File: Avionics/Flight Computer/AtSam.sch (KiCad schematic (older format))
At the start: 42 parts, among them U12 ATSAME70Q21A-AN, Y1 9HT11-32.768KDZB-T, Y2 7V-16.000MAHJ-T

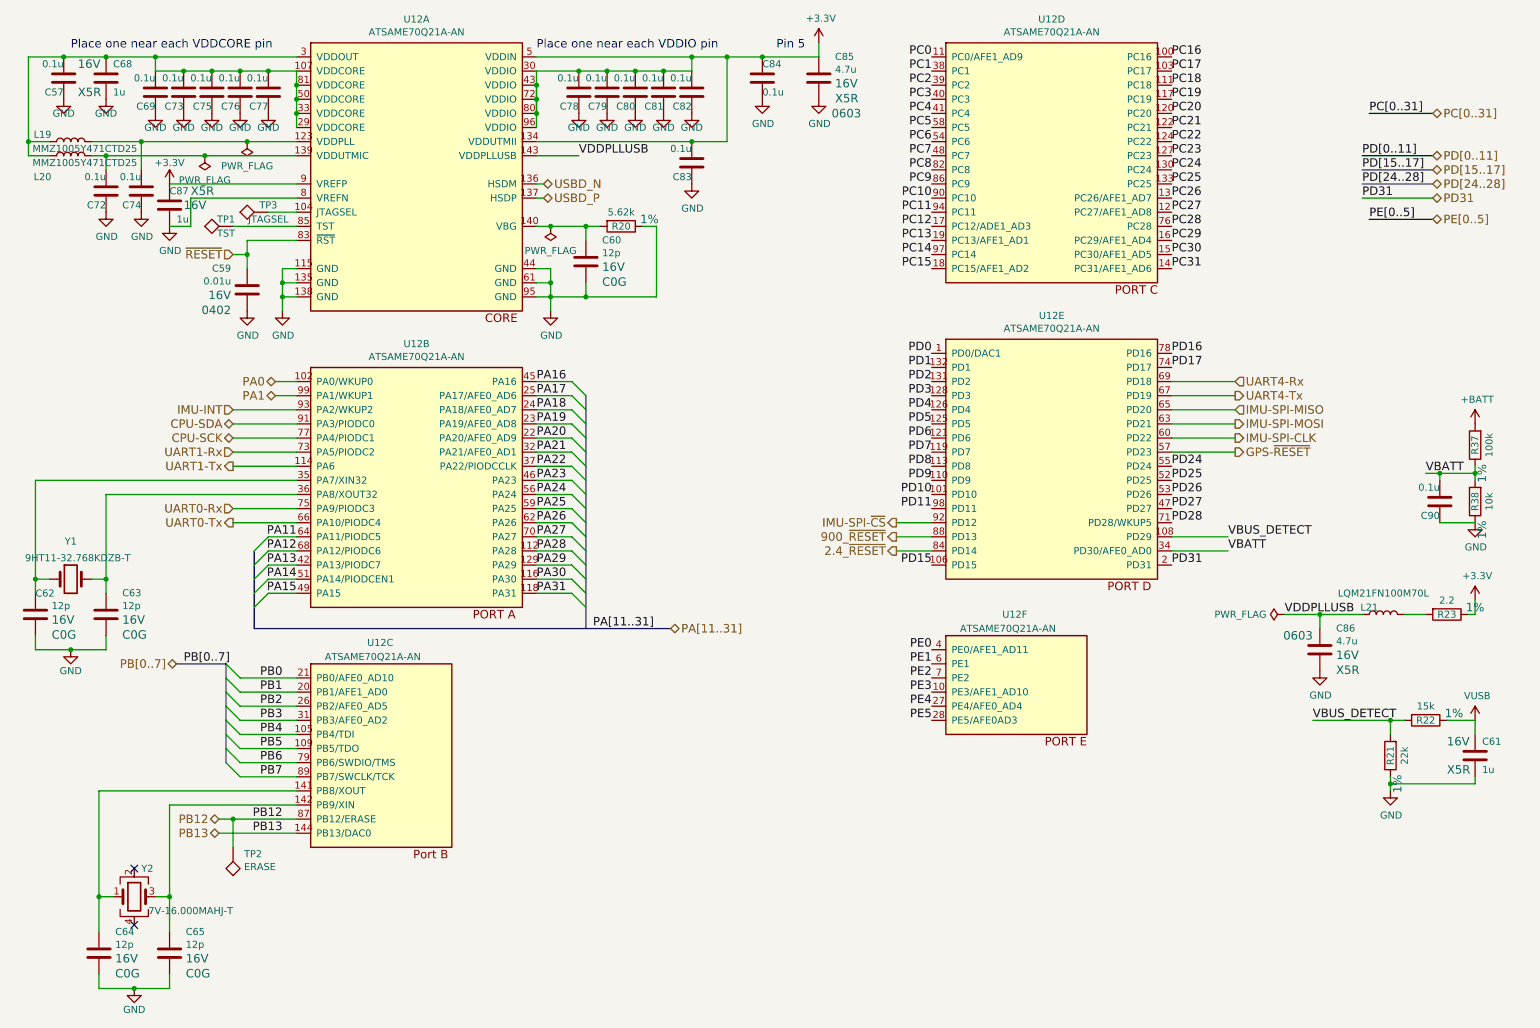
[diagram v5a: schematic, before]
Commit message: Built outputs and added manufacturing part numbers to make BOM search easier.
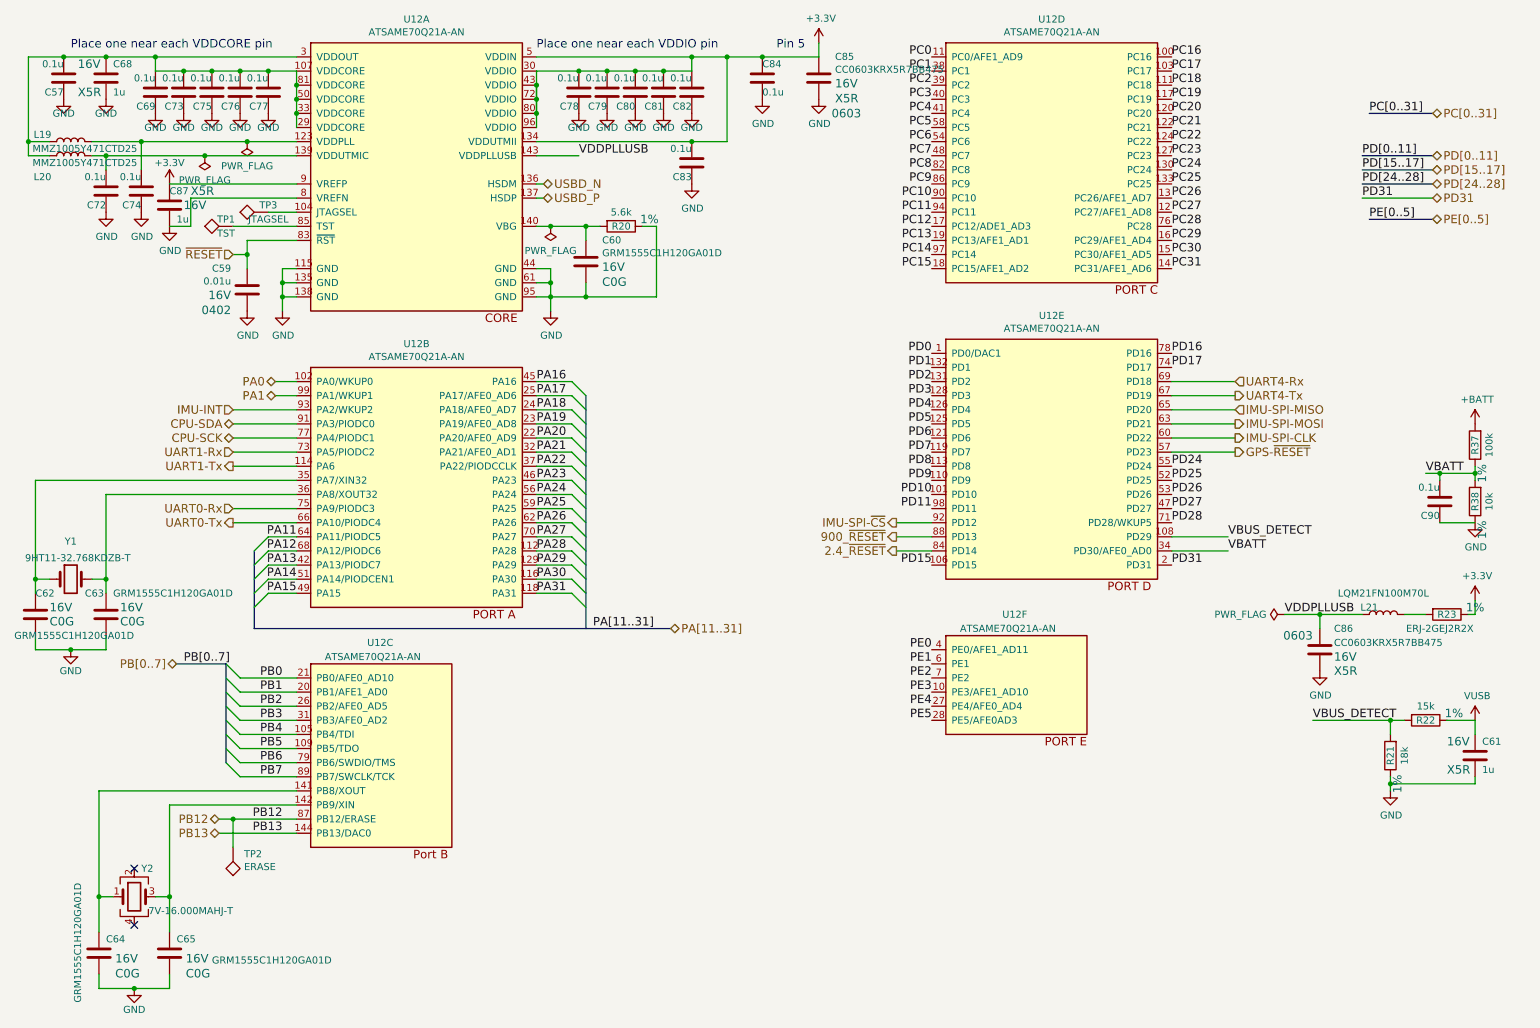
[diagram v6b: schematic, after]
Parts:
- C60, C62, C63, C64, C65: value 12p -> GRM1555C1H120GA01D
- C85, C86: value 4.7u -> CC0603KRX5R7BB475
- R20: value 5.62k -> 5.6k
- R21: value 22k -> 18k
- R23: value 2.2 -> ERJ-2GEJ2R2X
